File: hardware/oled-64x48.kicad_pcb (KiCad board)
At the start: 2 copper layers, 40 x 25 mm, 24 parts, among them P1 CON-SENSOR, U1 M24C64, U2 OLED066, U3 DRILL, U4 DRILL, U5 DRILL, U6 DRILL

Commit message: first prototype finished
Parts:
- moved VAL 12.2 mm to (151.7, 136.3)
- moved G*** 9.80 mm to (150.9, 130.6)
- moved G*** 4.60 mm to (165.9, 135.7)
- moved C10 0.60 mm to (144.2, 138.4)
- moved C2 0.60 mm to (159.9, 136.6)
- moved C3 0.60 mm to (159.7, 138.1)
- moved C4 0.60 mm to (156.6, 136.6)
- moved C5 0.60 mm to (156.8, 138.1)
- moved C6 0.60 mm to (146.5, 137.4)
- moved C7 0.60 mm to (162.7, 137.3)
- moved C8 0.60 mm to (144.0, 137.0)
- moved C9 0.60 mm to (164.5, 137.3)
- moved R1 0.60 mm to (148.8, 138.4)
- moved U2 0.60 mm to (154.1, 141.0)
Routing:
- net GND: track 84.1 -> 47.9 mm, vias 19 -> 23
- net Net-(P1-Pad8): track 2.67 -> 17.4 mm
- net Net-(P1-Pad10): track 5.62 -> 19.0 mm
- net Net-(P1-Pad7): track 13.0 -> 18.1 mm, vias 1 -> 0
- net 3V3: track 50.1 -> 48.7 mm, vias 2 -> 0
- net Net-(C6-Pad2): track 1.75 -> 2.99 mm
- net Net-(R1-Pad1): track 1.45 -> 2.66 mm
- net Net-(P1-Pad9): track 16.0 -> 16.5 mm, vias 1 -> 0
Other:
- board size 40 x 25 mm -> 35 x 25 mm
- board text added: "OLED 64x48"
- board text removed: "OLED 128x64"

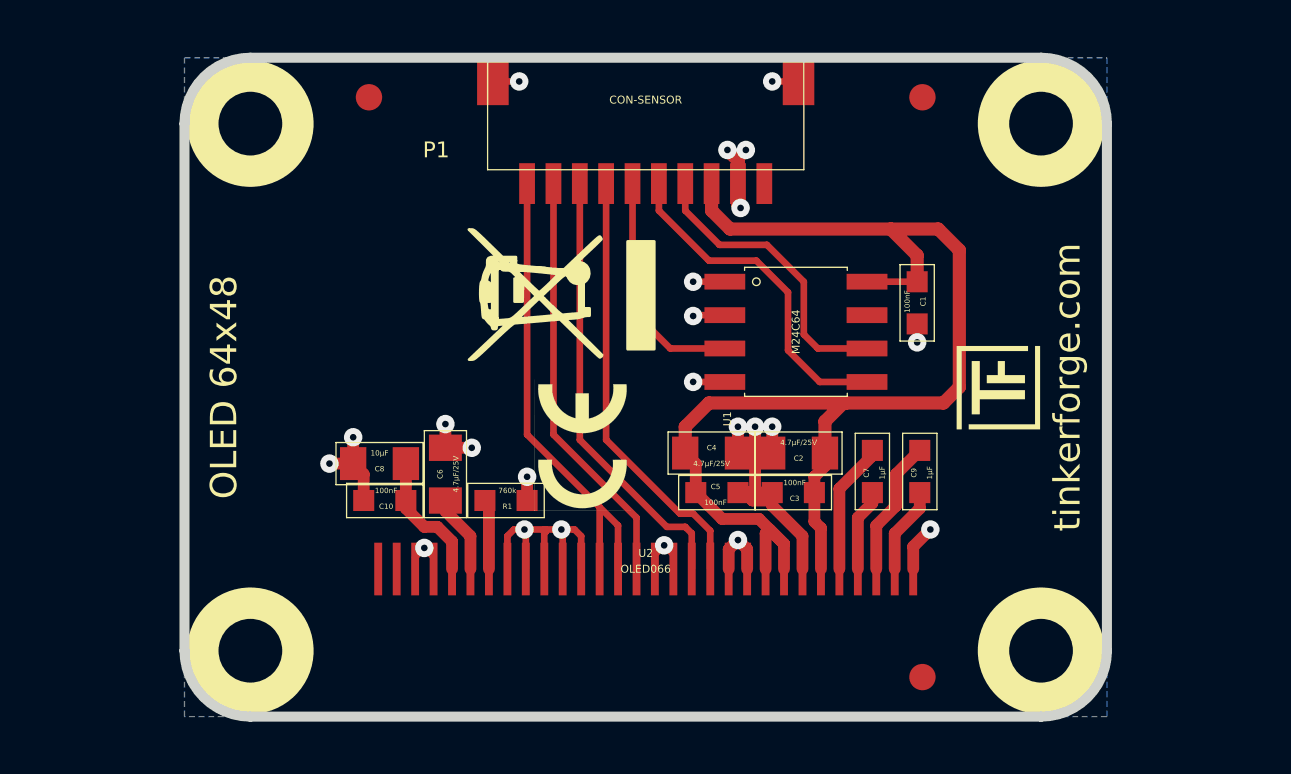
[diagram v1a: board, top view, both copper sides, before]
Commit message: change module size and text
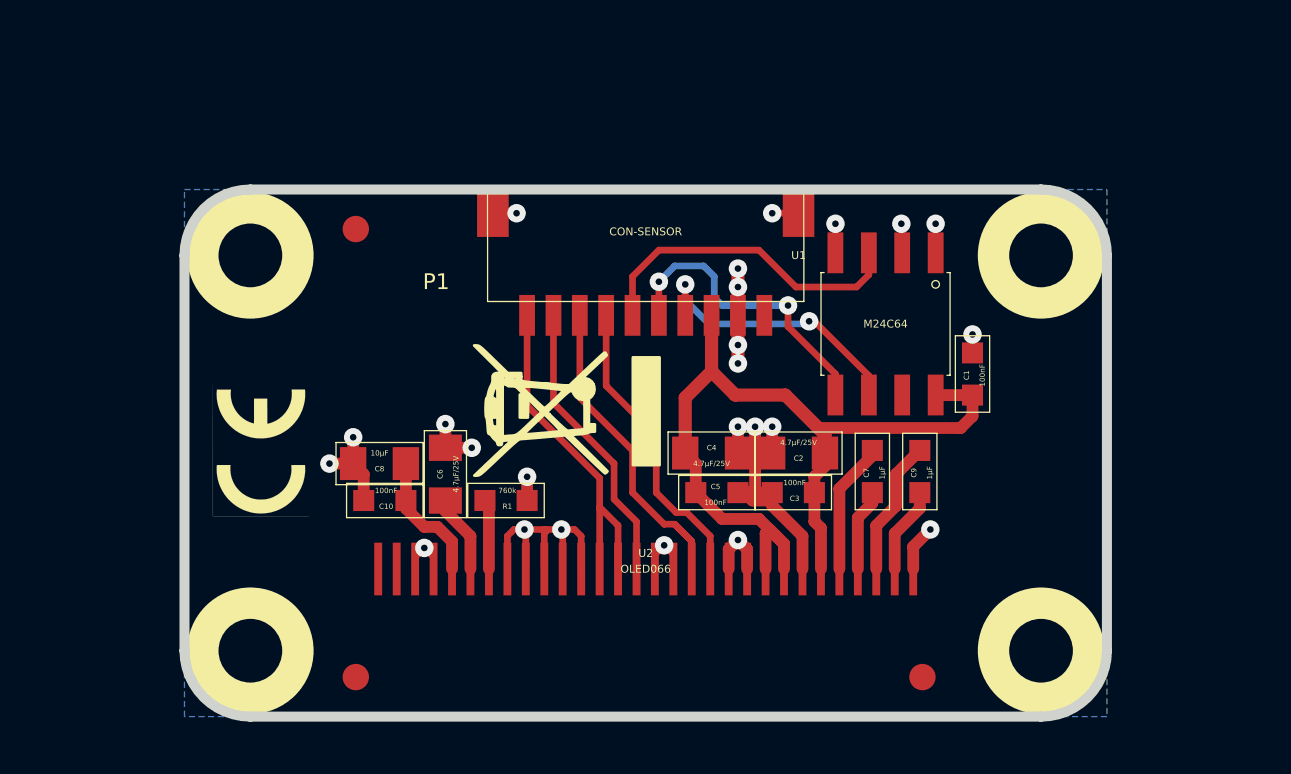
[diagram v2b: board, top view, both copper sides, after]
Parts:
- removed the G*** at (165.9, 135.7)
- added G***: LOGO, kicad-libraries:Logo_31x31m, B.Cu at (166.6, 135.0)
- moved Fiducial_Mark 30.8 mm to (143.1, 145.1)
- moved VAL 12.2 mm to (139.5, 136.5)
- moved Fiducial_Mark 5.02 mm to (143.1, 128.1)
- moved P1 5.00 mm to (154.1, 126.6)
- moved U4 5.00 mm to (139.1, 129.1)
- moved U5 5.00 mm to (169.1, 129.1)
- moved G*** 4.40 mm to (151.1, 135.0)
- moved C1 3.42 mm to (166.5, 133.6), turned to 270 degrees
- moved U1 3.41 mm to (163.2, 131.7), turned to 180 degrees
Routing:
- net 3V3: track 48.7 -> 33.6 mm
- net Net-(P1-Pad7): track 18.1 -> 11.5 mm
- net Net-(P1-Pad9): track 16.5 -> 10.9 mm
- net Net-(P1-Pad10): track 19.0 -> 13.4 mm
- net Net-(P1-Pad8): track 17.4 -> 12.5 mm
- net Net-(P1-Pad6): track 8.92 -> 12.5 mm
- net Net-(P1-Pad5): track 12.9 -> 11.7 mm, vias 0 -> 2
- net GND: track 47.9 -> 47.3 mm, vias 23 -> 24
- net Net-(P1-Pad4): track 11.3 -> 10.7 mm, vias 0 -> 2
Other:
- board size 35 x 25 mm -> 35 x 20 mm

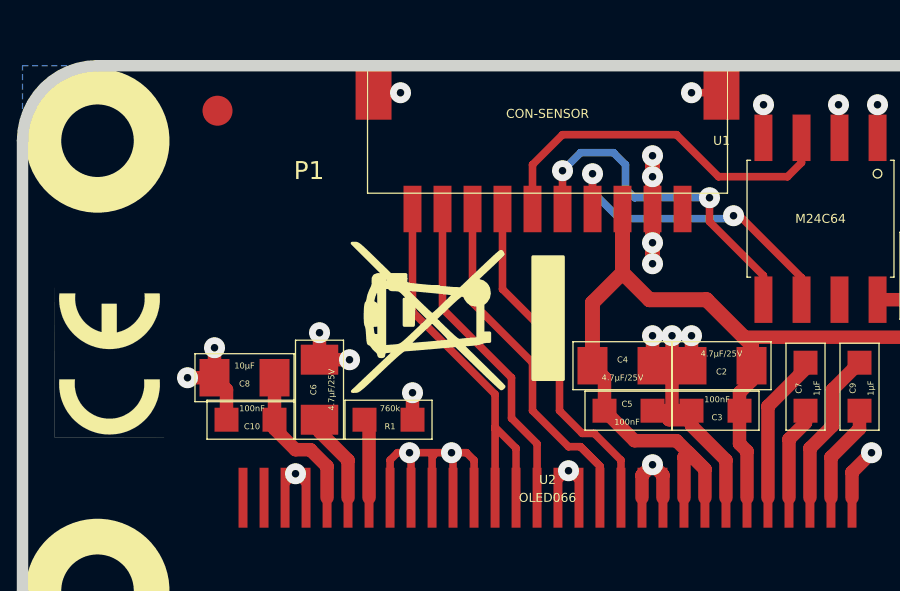
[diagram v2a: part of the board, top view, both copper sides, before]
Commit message: add i2c pullup
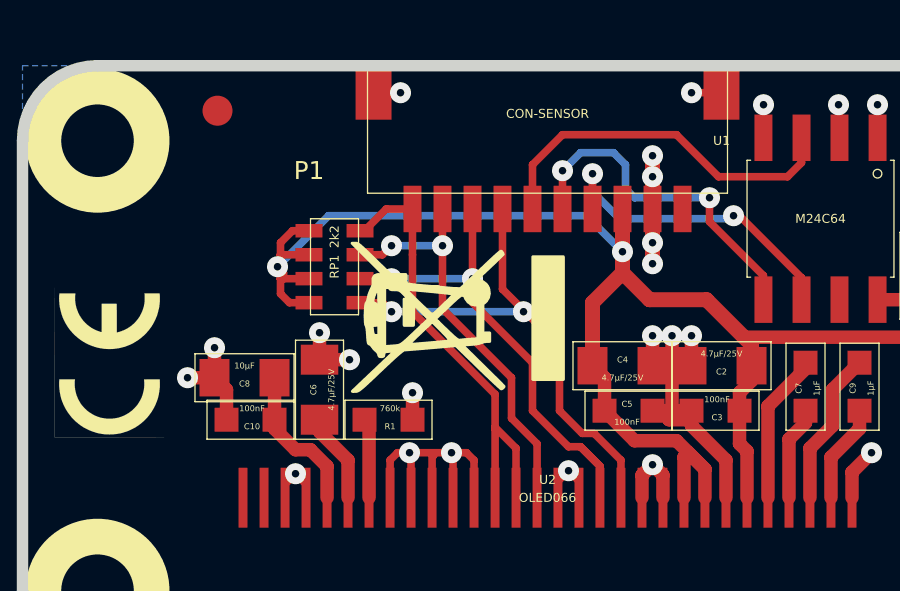
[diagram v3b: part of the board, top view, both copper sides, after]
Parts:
- added RP1: 2k2, kicad-libraries:0603X4, F.Cu at (147.0, 133.3)
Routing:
- net 3V3: track 33.6 -> 53.0 mm, vias 0 -> 2
- net Net-(P1-Pad7): track 11.5 -> 17.1 mm, vias 0 -> 2
- net Net-(P1-Pad8): track 12.5 -> 16.3 mm, vias 0 -> 2
- net Net-(P1-Pad9): track 10.9 -> 13.8 mm, vias 0 -> 2
- net Net-(P1-Pad10): track 13.4 -> 15.5 mm

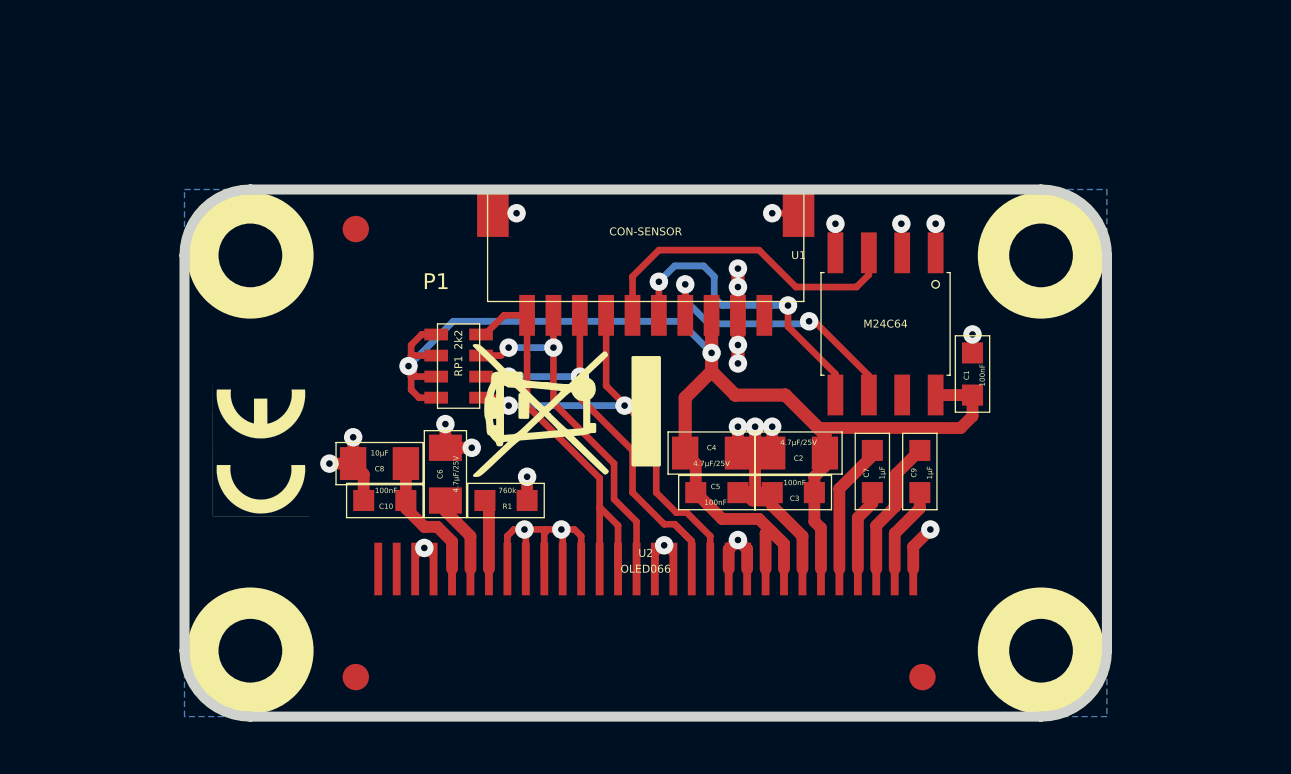
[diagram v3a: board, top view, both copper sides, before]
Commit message: change to 4-wire SPI, add nand for reset control
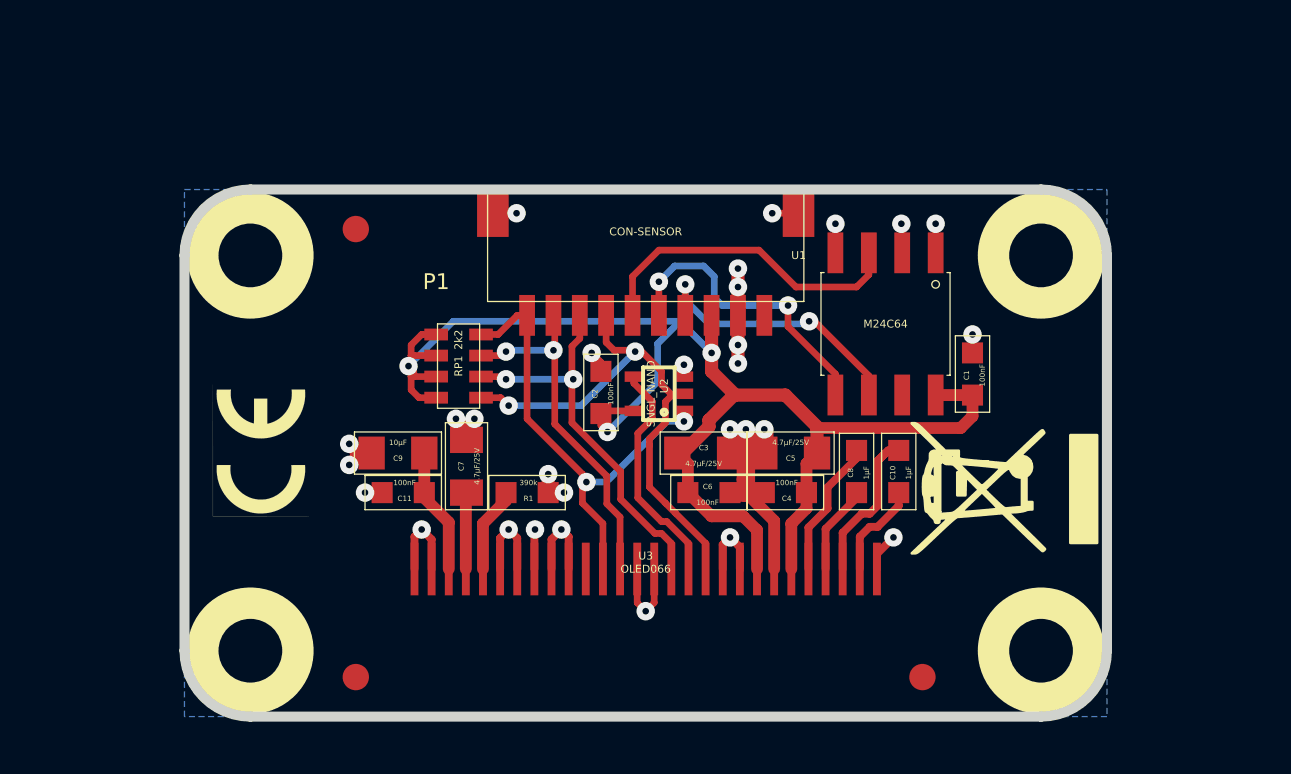
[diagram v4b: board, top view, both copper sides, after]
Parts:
- added C11: 100nF, kicad-libraries:0603, F.Cu at (144.9, 138.1)
- added U7: DRILL, kicad-libraries:DRILL_NP, F.Cu at (139.1, 144.1)
- C10: value 100nF -> 1µF
- C2, C4, C6: value 4.7µF/25V -> 100nF; footprint kicad-libraries:0805 -> kicad-libraries:0603
- C3, C5: value 100nF -> 4.7µF/25V; footprint kicad-libraries:0603 -> kicad-libraries:0805
- C7: value 1µF -> 4.7µF/25V; footprint kicad-libraries:0603 -> kicad-libraries:0805
- C8: value 10µF -> 1µF; footprint kicad-libraries:0805 -> kicad-libraries:0603
- C9: value 1µF -> 10µF; footprint kicad-libraries:0603 -> kicad-libraries:0805
- R1: value 760k -> 390k
- U2: value OLED066 -> SNGL_NAND; footprint kicad-libraries:OLED013 -> kicad-libraries:SC70-5
- U3: value DRILL -> OLED066; footprint kicad-libraries:DRILL_NP -> kicad-libraries:OLED066
- moved C9 19.8 mm to (144.7, 136.6), turned to 0 degrees
- moved C10 19.5 mm to (163.7, 137.3), turned to 270 degrees
- moved C8 18.1 mm to (162.1, 137.3), turned to 270 degrees
- moved G*** 16.9 mm to (167.7, 137.9)
- moved C7 15.4 mm to (147.3, 137.1)
- moved U3 15.3 mm to (154.1, 141.0), turned to 180 degrees
- moved C6 10.0 mm to (156.5, 138.1), turned to 180 degrees
- moved C2 7.84 mm to (152.4, 134.3), turned to 270 degrees
- moved U2 6.67 mm to (154.6, 134.3), turned to 90 degrees
- moved C3 3.72 mm to (156.3, 136.6), turned to 180 degrees
- moved C4 3.18 mm to (159.4, 138.1), turned to 0 degrees
- moved C5 3.18 mm to (159.6, 136.6), turned to 0 degrees
- moved R1 0.85 mm to (149.6, 138.1)
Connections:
- C10 pad 1: GND -> Net-(C10-Pad1)
- C6 pad 2: Net-(C6-Pad2) -> 3V3
- C7 pad 1: Net-(C7-Pad1) -> GND
- C8 pad 1: GND -> Net-(C8-Pad1)
- C8 pad 2: Net-(C10-Pad2) -> Net-(C8-Pad2)
- C9 pad 1: Net-(C9-Pad1) -> GND
- C9 pad 2: Net-(C9-Pad2) -> Net-(C11-Pad2)
- U2 pad 1: GND -> Net-(P1-Pad10)
- U2 pad 2: Net-(C9-Pad2) -> Net-(P1-Pad7)
- U2 pad 3: Net-(C9-Pad1) -> GND
- U2 pad 4: Net-(C7-Pad2) -> Net-(U2-Pad4)
- U2 pad 5: Net-(C7-Pad1) -> 3V3
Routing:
- net Net-(U2-Pad4): track 0.00 -> 8.68 mm
- net Net-(C10-Pad1): track 0.00 -> 6.22 mm
- net Net-(C8-Pad1): track 0.00 -> 5.26 mm
- net Net-(C9-Pad1): track 5.18 -> 0.00 mm
- net Net-(C7-Pad1): track 5.02 -> 0.00 mm
- net Net-(C11-Pad2): track 0.00 -> 4.78 mm
- net 3V3: track 53.0 -> 57.5 mm, vias 2 -> 3
- net Net-(C8-Pad2): track 0.00 -> 3.47 mm
- net Net-(C9-Pad2): track 3.29 -> 0.00 mm
- net Net-(C6-Pad2): track 2.99 -> 0.00 mm
- net Net-(P1-Pad10): track 15.5 -> 18.4 mm, vias 0 -> 2
- net Net-(P1-Pad7): track 17.1 -> 20.0 mm
- net GND: track 47.3 -> 49.6 mm, vias 24 -> 29
- net Net-(C10-Pad2): track 5.02 -> 3.69 mm
- net Net-(P1-Pad8): track 16.3 -> 15.1 mm
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
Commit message: change pullup resistor to series resistor, fix routing
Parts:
- RP1: value 2k2 -> 220
- moved RP1 7.66 mm to (153.1, 138.0), turned to 0 degrees
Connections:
- RP1 pad 1: 3V3 -> Net-(P1-Pad7)
- RP1 pad 2: 3V3 -> Net-(P1-Pad8)
- RP1 pad 3: 3V3 -> Net-(P1-Pad9)
- RP1 pad 4: 3V3 -> Net-(P1-Pad10)
- RP1 pad 5: Net-(P1-Pad7) -> Net-(RP1-Pad5)
- RP1 pad 6: Net-(P1-Pad8) -> Net-(RP1-Pad6)
- RP1 pad 7: Net-(P1-Pad9) -> Net-(RP1-Pad7)
- RP1 pad 8: Net-(P1-Pad10) -> Net-(RP1-Pad8)
- U3 pad 11: Net-(P1-Pad7) -> Net-(RP1-Pad8)
- U3 pad 13: Net-(P1-Pad8) -> Net-(RP1-Pad7)
- U3 pad 16: Net-(P1-Pad9) -> Net-(RP1-Pad6)
- U3 pad 17: Net-(P1-Pad10) -> Net-(RP1-Pad5)
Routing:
- net 3V3: track 57.5 -> 38.8 mm, vias 3 -> 2
- net Net-(P1-Pad7): track 20.0 -> 8.23 mm, vias 2 -> 0
- net Net-(P1-Pad8): track 15.1 -> 7.99 mm, vias 2 -> 0
- net Net-(P1-Pad9): track 13.6 -> 7.59 mm, vias 2 -> 0
- net Net-(P1-Pad10): track 18.4 -> 12.8 mm
- net Net-(U2-Pad4): track 8.68 -> 12.6 mm, vias 0 -> 2
- net Net-(RP1-Pad7): track 0.00 -> 3.86 mm
- net Net-(RP1-Pad8): track 0.00 -> 3.79 mm
- net Net-(RP1-Pad5): track 0.00 -> 2.33 mm
- net Net-(RP1-Pad6): track 0.00 -> 2.27 mm

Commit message: add hardware version number
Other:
- board text added: "OLED 64x48 1.0"
- board text removed: "OLED 64x48"
